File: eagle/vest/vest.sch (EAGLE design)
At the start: 20 parts, among them IC1 74HCT245

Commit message: wip
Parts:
- added C2, C3, C4, C5: (no value), rcl:C-EU025-025X050
- added C6: 470uF, rcl:CPOL-USTT2D7L
- added JP1: (no value), microbuilder:HEADER-1X870MIL
- added PWR+, PWR-: WIREPAD4,16O1,6, wirepad:WIREPAD4,16O1,6
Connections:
- new net 3.3V: J1.7, J1.8, JP1.7, JP1.8, U$1.3.3V
- net BTN1: now also C5.1, JP1.5, U$1.18/A4/T/SDA0
- net BTN2: now also C4.1, JP1.6, U$1.19/A5/T/SCL0
- net GND: now also C2.2, C3.2, C4.2, C5.2, C6.-, JP1.2, JP1.4, PWR-.P
- net POT1: now also C2.1, JP1.1, U$1.22/A8/T/PWM
- net POT2: now also C3.1, JP1.3, U$1.23/A9/T/PWM
- net VCC: now also C6.+, PWR+.P; no longer J1.7, J1.8

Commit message: vest before autorouter
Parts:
- added AUX1, AUX2: (no value), microbuilder:HEADER-1X3
- added H1, H2, H3, H4: MOUNT-HOLE3.0, holes:MOUNT-HOLE3.0
- R1, R2, R3, R4, R5, R6, R7, R8: device rcl:R-US_0207/10 -> rcl:R-US_0204/7
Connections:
- new net AUX1: AUX1.2, U$1.12/MISO
- new net AUX2: AUX2.2, U$1.17/A3/T
- net GND: now also AUX1.1, AUX2.1
- net VCC: now also AUX1.3, AUX2.3

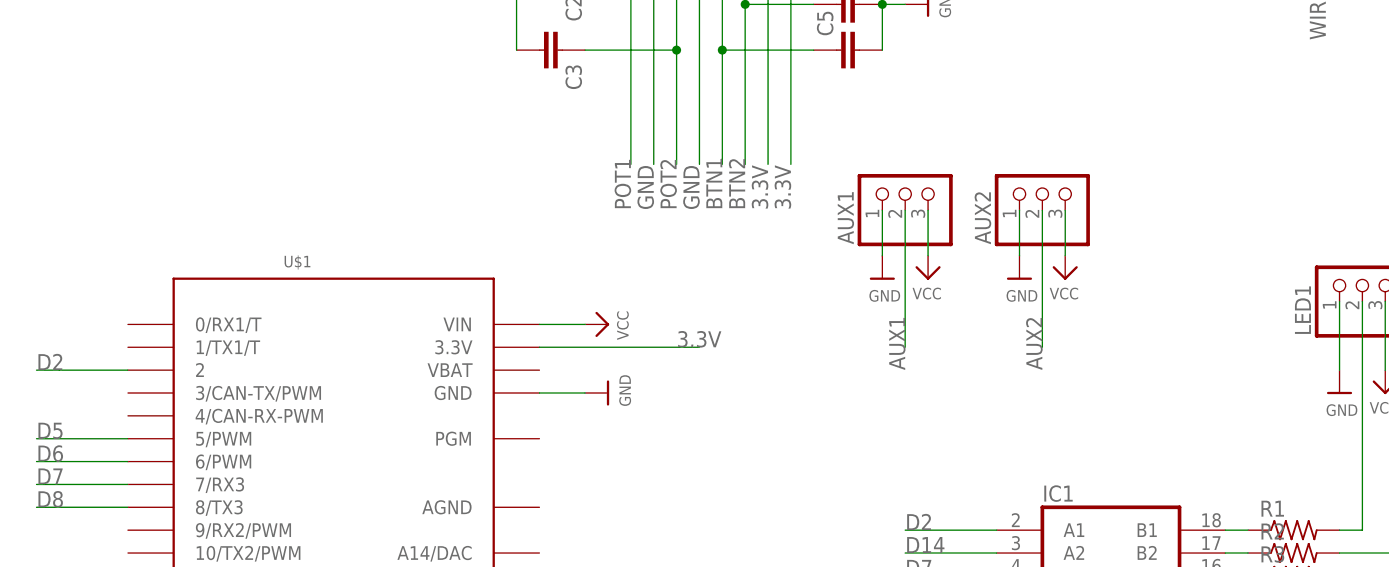
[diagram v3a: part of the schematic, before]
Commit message: jacket teensy code 'ported' from pants - works but timing sux
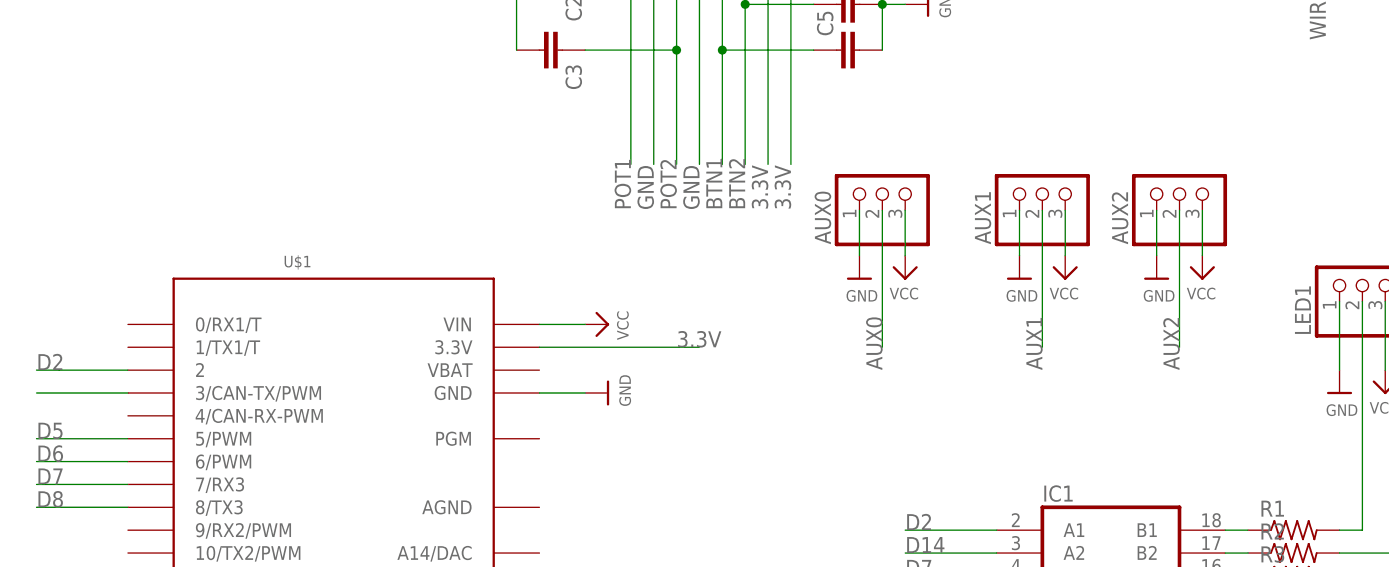
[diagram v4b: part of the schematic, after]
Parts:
- added AUX0: (no value), microbuilder:HEADER-1X3
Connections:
- new net AUX0: AUX0.2, U$1.3/CAN-TX/PWM
- net GND: now also AUX0.1
- net VCC: now also AUX0.3
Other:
- moved on the sheet: AUX1, AUX2
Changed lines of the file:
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@@
 <grid distance="0.1" unitdist="inch" unit="inch" style="lines" multiple="1" display="no" altdistance="0.01" altunitdist="inch" altunit="inch"/>
 <layers>
-<layer number="1" name="Top" color="4" fill="1" visible="yes" active="no"/>
-<layer number="16" name="Bottom" color="1" fill="1" visible="yes" active="no"/>
-<layer number="17" name="Pads" color="2" fill="1" visible="yes" active="no"/>
-<layer number="18" name="Vias" color="2" fill="1" visible="yes" active="no"/>
-<layer number="19" name="Unrouted" color="6" fill="1" visible="yes" active="no"/>
-<layer number="20" name="Dimension" color="15" fill="1" visible="yes" active="no"/>
-<layer number="21" name="tPlace" color="7" fill="1" visible="yes" active="no"/>
-<layer number="22" name="bPlace" color="7" fill="1" visible="yes" active="no"/>
-<layer number="23" name="tOrigins" color="15" fill="1" visible="yes" active="no"/>
-<layer number="24" name="bOrigins" color="15" fill="1" visible="yes" active="no"/>
-<layer number="25" name="tNames" color="7" fill="1" visible="yes" active="no"/>
-<layer number="26" name="bNames" color="7" fill="1" visible="yes" active="no"/>
-<layer number="27" name="tValues" color="7" fill="1" visible="yes" active="no"/>
-<layer number="28" name="bValues" color="7" fill="1" visible="yes" active="no"/>
+<layer number="1" name="Top" color="4" fill="1" visible="no" active="no"/>
+<layer number="16" name="Bottom" color="1" fill="1" visible="no" active="no"/>
+<layer number="17" name="Pads" color="2" fill="1" visible="no" active="no"/>
+<layer number="18" name="Vias" color="2" fill="1" visible="no" active="no"/>
+<layer number="19" name="Unrouted" color="6" fill="1" visible="no" active="no"/>
+<layer number="20" name="Dimension" color="15" fill="1" visible="no" active="no"/>
+<layer number="21" name="tPlace" color="7" fill="1" visible="no" active="no"/>
+<layer number="22" name="bPlace" color="7" fill="1" visible="no" active="no"/>
+<layer number="23" name="tOrigins" color="15" fill="1" visible="no" active="no"/>
+<layer number="24" name="bOrigins" color="15" fill="1" visible="no" active="no"/>
+<layer number="25" name="tNames" color="7" fill="1" visible="no" active="no"/>
+<layer number="26" name="bNames" color="7" fill="1" visible="no" active="no"/>
+<layer number="27" name="tValues" color="7" fill="1" visible="no" active="no"/>
+<layer number="28" name="bValues" color="7" fill="1" visible="no" active="no"/>
 <layer number="29" name="tStop" color="7" fill="3" visible="no" active="no"/>
 <layer number="30" name="bStop" color="7" fill="6" visible="no" active="no"/>
@@
 <layer number="35" name="tGlue" color="7" fill="4" visible="no" active="no"/>
 <layer number="36" name="bGlue" color="7" fill="5" visible="no" active="no"/>
-<layer number="37" name="tTest" color="7" fill="1" visible="yes" active="no"/>
-<layer number="38" name="bTest" color="7" fill="1" visible="yes" active="no"/>
+<layer number="37" name="tTest" color="7" fill="1" visible="no" active="no"/>
+<layer number="38" name="bTest" color="7" fill="1" visible="no" active="no"/>
 <layer number="39" name="tKeepout" color="4" fill="11" visible="no" active="no"/>
 <layer number="40" name="bKeepout" color="1" fill="11" visible="no" active="no"/>
@@
 <layer number="44" name="Drills" color="7" fill="1" visible="no" active="no"/>
 <layer number="45" name="Holes" color="7" fill="1" visible="no" active="no"/>
-<layer number="46" name="Milling" color="3" fill="1" visible="yes" active="no"/>
-<layer number="47" name="Measures" color="7" fill="1" visible="yes" active="no"/>
-<layer number="48" name="Document" color="7" fill="1" visible="yes" active="no"/>
-<layer number="49" name="Reference" color="7" fill="1" visible="yes" active="no"/>
-<layer number="50" name="dxf" color="7" fill="1" visible="yes" active="no"/>
-<layer number="51" name="tDocu" color="7" fill="1" visible="yes" active="no"/>
-<layer number="52" name="bDocu" color="7" fill="1" visible="yes" active="no"/>
-<layer number="53" name="tGND_GNDA" color="7" fill="9" visible="yes" active="no"/>
-<layer number="54" name="bGND_GNDA" color="1" fill="9" visible="yes" active="no"/>
-<layer number="56" name="wert" color="7" fill="1" visible="yes" active="no"/>
+<layer number="46" name="Milling" color="3" fill="1" visible="no" active="no"/>
+<layer number="47" name="Measures" color="7" fill="1" visible="no" active="no"/>
+<layer number="48" name="Document" color="7" fill="1" visible="no" active="no"/>
+<layer number="49" name="Reference" color="7" fill="1" visible="no" active="no"/>
+<layer number="50" name="dxf" color="7" fill="1" visible="no" active="no"/>
+<layer number="51" name="tDocu" color="7" fill="1" visible="no" active="no"/>
+<layer number="52" name="bDocu" color="7" fill="1" visible="no" active="no"/>
+<layer number="53" name="tGND_GNDA" color="7" fill="9" visible="no" active="no"/>
+<layer number="54" name="bGND_GNDA" color="1" fill="9" visible="no" active="no"/>
+<layer number="56" name="wert" color="7" fill="1" visible="no" active="no"/>
 <layer number="91" name="Nets" color="2" fill="1" visible="yes" active="yes"/>
 <layer number="92" name="Busses" color="1" fill="1" visible="yes" active="yes"/>
@@
 <part name="H3" library="holes" deviceset="MOUNT-HOLE" device="3.0"/>
 <part name="H4" library="holes" deviceset="MOUNT-HOLE" device="3.0"/>
+<part name="AUX0" library="microbuilder" deviceset="HEADER-1X3" device=""/>
+<part name="P+16" library="microbuilder" deviceset="VCC" device=""/>
+<part name="U$19" library="microbuilder" deviceset="GND" device=""/>
 </parts>
 <sheets>
@@
 <instance part="P+13" gate="VCC" x="195.58" y="139.7"/>
 <instance part="U$16" gate="G$1" x="195.58" y="121.92"/>
-<instance part="AUX1" gate="A" x="121.92" y="101.6" rot="R90"/>
-<instance part="AUX2" gate="A" x="137.16" y="101.6" rot="R90"/>
-<instance part="P+14" gate="VCC" x="139.7" y="91.44" rot="R180"/>
-<instance part="P+15" gate="VCC" x="124.46" y="91.44" rot="R180"/>
-<instance part="U$17" gate="G$1" x="134.62" y="91.44"/>
-<instance part="U$18" gate="G$1" x="119.38" y="91.44"/>
+<instance part="AUX1" gate="A" x="137.16" y="101.6" rot="R90"/>
+<instance part="AUX2" gate="A" x="152.4" y="101.6" rot="R90"/>
+<instance part="P+14" gate="VCC" x="154.94" y="91.44" rot="R180"/>
+<instance part="P+15" gate="VCC" x="139.7" y="91.44" rot="R180"/>
+<instance part="U$17" gate="G$1" x="149.86" y="91.44"/>
+<instance part="U$18" gate="G$1" x="134.62" y="91.44"/>
 <instance part="H1" gate="G$1" x="30.48" y="144.78"/>
 <instance part="H2" gate="G$1" x="25.4" y="134.62"/>
 <instance part="H3" gate="G$1" x="48.26" y="144.78"/>
 <instance part="H4" gate="G$1" x="35.56" y="132.08"/>
+<instance part="AUX0" gate="A" x="119.38" y="101.6" rot="R90"/>
+<instance part="P+16" gate="VCC" x="121.92" y="91.44" rot="R180"/>
+<instance part="U$19" gate="G$1" x="116.84" y="91.44"/>
 </instances>
 <busses>
@@
 <pinref part="AUX1" gate="A" pin="1"/>
 <pinref part="U$18" gate="G$1" pin="GND"/>
-<wire x1="119.38" y1="99.06" x2="119.38" y2="93.98" width="0.1524" layer="91"/>
+<wire x1="134.62" y1="99.06" x2="134.62" y2="93.98" width="0.1524" layer="91"/>
 </segment>
 <segment>
 <pinref part="AUX2" gate="A" pin="1"/>
 <pinref part="U$17" gate="G$1" pin="GND"/>
-<wire x1="134.62" y1="99.06" x2="134.62" y2="93.98" width="0.1524" layer="91"/>
+<wire x1="149.86" y1="99.06" x2="149.86" y2="93.98" width="0.1524" layer="91"/>
+</segment>
+<segment>
+<pinref part="AUX0" gate="A" pin="1"/>
+<pinref part="U$19" gate="G$1" pin="GND"/>
+<wire x1="116.84" y1="99.06" x2="116.84" y2="93.98" width="0.1524" layer="91"/>
 </segment>
 </net>
@@
 <pinref part="AUX1" gate="A" pin="3"/>
 <pinref part="P+15" gate="VCC" pin="VCC"/>
-<wire x1="124.46" y1="99.06" x2="124.46" y2="93.98" width="0.1524" layer="91"/>
+<wire x1="139.7" y1="99.06" x2="139.7" y2="93.98" width="0.1524" layer="91"/>
 </segment>
 <segment>
 <pinref part="AUX2" gate="A" pin="3"/>
 <pinref part="P+14" gate="VCC" pin="VCC"/>
-<wire x1="139.7" y1="99.06" x2="139.7" y2="93.98" width="0.1524" layer="91"/>
+<wire x1="154.94" y1="99.06" x2="154.94" y2="93.98" width="0.1524" layer="91"/>
+</segment>
+<segment>
+<pinref part="AUX0" gate="A" pin="3"/>
+<pinref part="P+16" gate="VCC" pin="VCC"/>
+<wire x1="121.92" y1="99.06" x2="121.92" y2="93.98" width="0.1524" layer="91"/>
 </segment>
 </net>
@@
 <segment>
 <pinref part="AUX1" gate="A" pin="2"/>
-<wire x1="121.92" y1="99.06" x2="121.92" y2="83.82" width="0.1524" layer="91"/>
-<label x="121.92" y="81.28" size="1.778" layer="95" rot="R90"/>
+<wire x1="137.16" y1="99.06" x2="137.16" y2="83.82" width="0.1524" layer="91"/>
+<label x="137.16" y="81.28" size="1.778" layer="95" rot="R90"/>
 </segment>
 <segment>
@@
 <segment>
 <pinref part="AUX2" gate="A" pin="2"/>
-<wire x1="137.16" y1="99.06" x2="137.16" y2="83.82" width="0.1524" layer="91"/>
-<label x="137.16" y="81.28" size="1.778" layer="95" rot="R90"/>
+<wire x1="152.4" y1="99.06" x2="152.4" y2="83.82" width="0.1524" layer="91"/>
+<label x="152.4" y="81.28" size="1.778" layer="95" rot="R90"/>
 </segment>
 <segment>
@@
 </segment>
 </net>
+<net name="AUX0" class="0">
+<segment>
+<pinref part="AUX0" gate="A" pin="2"/>
+<wire x1="119.38" y1="99.06" x2="119.38" y2="83.82" width="0.1524" layer="91"/>
+<label x="119.38" y="81.28" size="1.778" layer="95" rot="R90"/>
+</segment>
+<segment>
+<pinref part="U$1" gate="G$1" pin="3/CAN-TX/PWM"/>
+<wire x1="35.56" y1="78.74" x2="25.4" y2="78.74" width="0.1524" layer="91"/>
+</segment>
+</net>
